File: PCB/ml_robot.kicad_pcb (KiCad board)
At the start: 2 copper layers, 85.4 x 100 mm, 17 parts, among them J1 lidar_conn, J2 Motor1, J3 Motor2, J4 jmp_alim, J5 ext_power, SW1 SW_Push, U1 ESP32-S3-DEVKITC-1-N8R2, U3 TB6612FNG

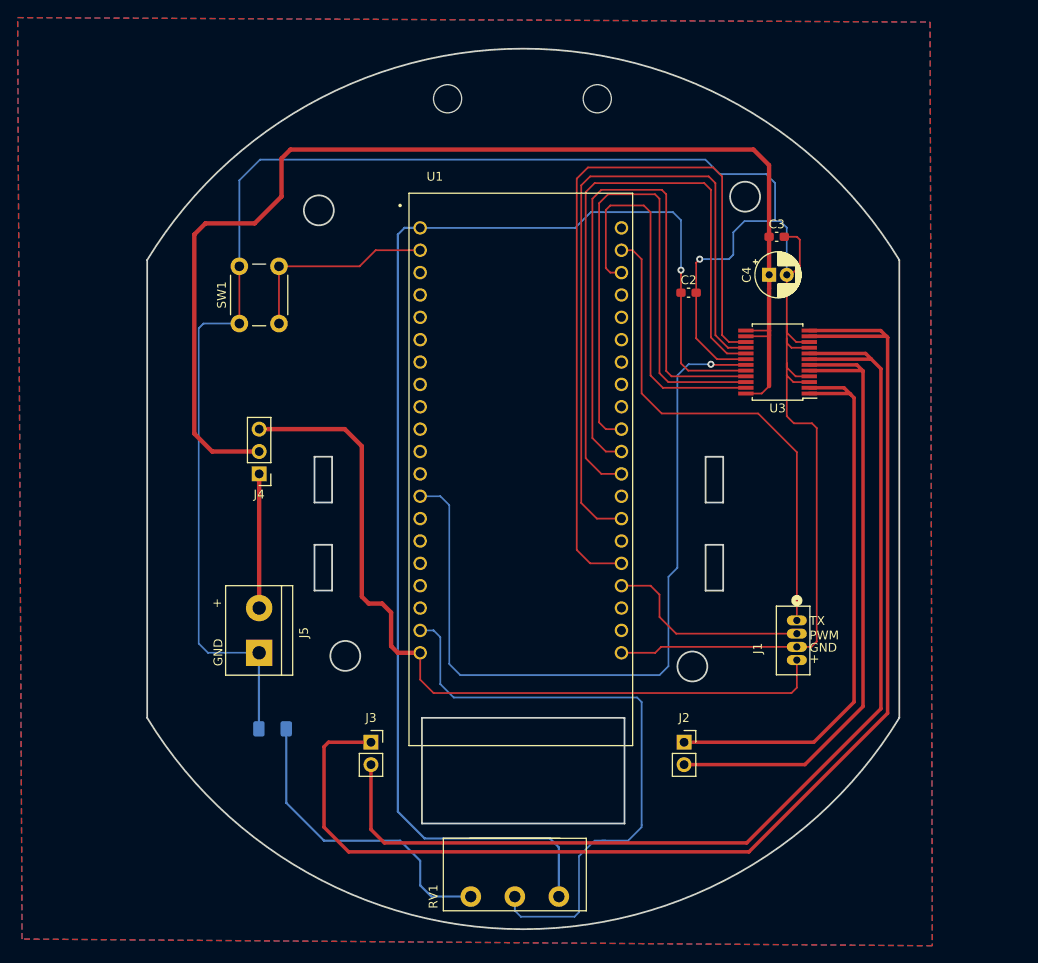
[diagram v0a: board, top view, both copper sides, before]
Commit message: Adding exclusion zones
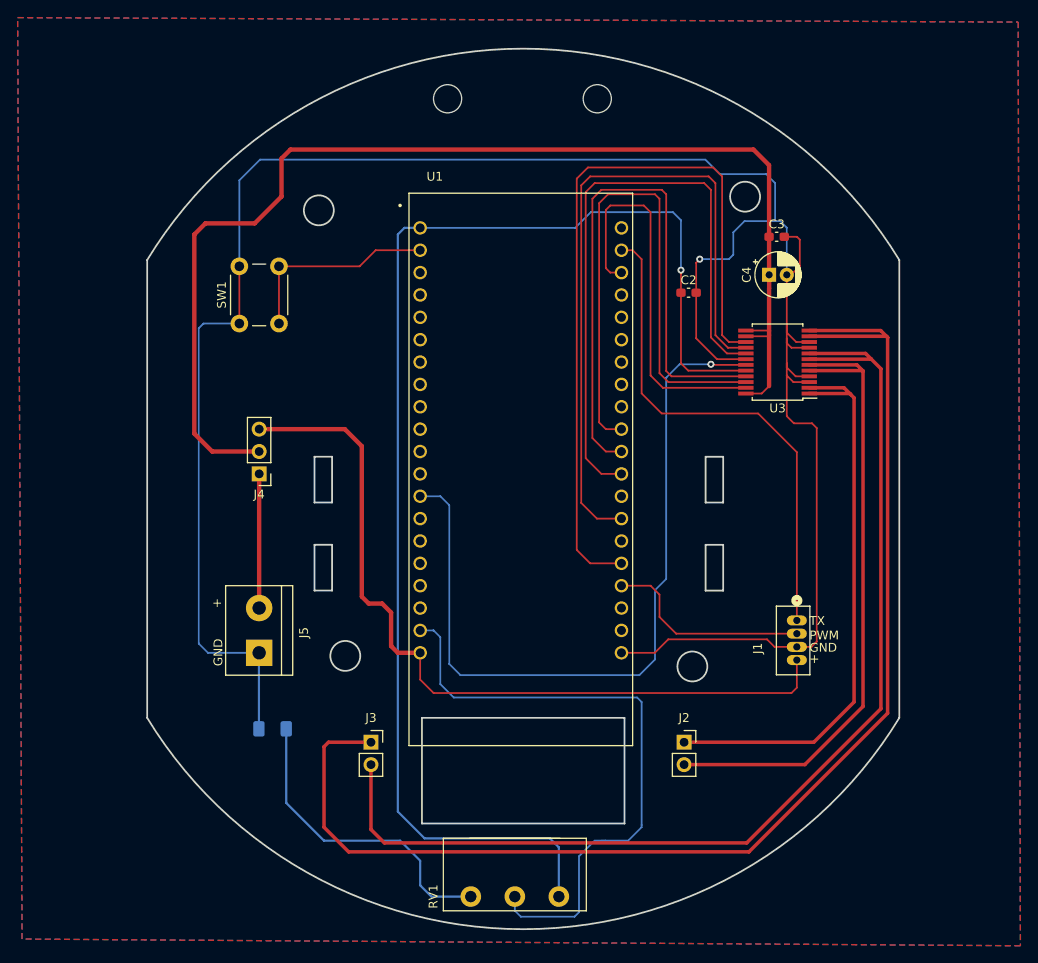
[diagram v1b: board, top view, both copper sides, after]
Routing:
- net /STBY_motor: track 89.4 -> 88.6 mm
- net GND: track 261.9 -> 262.7 mm
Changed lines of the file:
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@@
   )
   (paper "A4")
+  (title_block
+    (title "machine_learning_robot")
+    (date "2023-10-05")
+    (rev "A1")
+    (company "Institute for Future Technologies")
+    (comment 2 "Co-Author : Nicolas STAS")
+    (comment 3 "Author : Matthieu SEGUI")
+  )
   (layers
     (0 "F.Cu" signal)
@@
   (segment (start 139.2682 71.882) (end 148.59 71.882) (width 0.2) (layer "B.Cu") (net 1))
   (segment (start 162.534 90.525) (end 161.519888 89.510888) (width 0.2) (layer "F.Cu") (net 2))
+  (segment (start 142.748 121.922) (end 146.5306 121.922) (width 0.2) (layer "F.Cu") (net 2))
   (segment (start 164.3241 121.2481) (end 164.9222 120.65) (width 0.2) (layer "F.Cu") (net 2))
   (segment (start 161.519888 95.048088) (end 161.519888 90.425288) (width 0.2) (layer "F.Cu") (net 2))
   (segment (start 164.075 87.275) (end 162.0526 87.275) (width 0.2) (layer "F.Cu") (net 2))
+  (segment (start 159.2834 120.396) (end 160.1355 121.2481) (width 0.2) (layer "F.Cu") (net 2))
   (segment (start 151.2305 86.2065) (end 151.2305 81.026) (width 0.2) (layer "F.Cu") (net 2))
+  (segment (start 160.1355 121.2481) (end 162.6645 121.2481) (width 0.2) (layer "F.Cu") (net 2))
   (segment (start 164.3888 95.8596) (end 162.3314 95.8596) (width 0.2) (layer "F.Cu") (net 2))
   (segment (start 99.35 84.53) (end 99.35 78.03) (width 0.2) (layer "F.Cu") (net 2))
@@
   (segment (start 156.875 88.575) (end 153.599 88.575) (width 0.2) (layer "F.Cu") (net 2))
   (segment (start 162.5964 86.625) (end 161.519888 85.548488) (width 0.2) (layer "F.Cu") (net 2))
-  (segment (start 146.5814 121.922) (end 142.748 121.922) (width 0.2) (layer "F.Cu") (net 2))
+  (segment (start 146.5306 121.922) (end 148.0566 120.396) (width 0.2) (layer "F.Cu") (net 2))
   (segment (start 161.519888 90.425288) (end 161.519888 89.0524) (width 0.2) (layer "F.Cu") (net 2))
   (segment (start 162.6645 121.2481) (end 164.3241 121.2481) (width 0.2) (layer "F.Cu") (net 2))
+  (segment (start 162.6645 121.2481) (end 162.6626 121.25) (width 0.2) (layer "F.Cu") (net 2))
+  (segment (start 148.0566 120.396) (end 159.2834 120.396) (width 0.2) (layer "F.Cu") (net 2))
   (segment (start 161.519888 84.6836) (end 161.519888 78.994) (width 0.2) (layer "F.Cu") (net 2))
   (segment (start 151.2305 77.6235) (end 151.638 77.216) (width 0.2) (layer "F.Cu") (net 2))
@@
   (segment (start 161.237 74.676) (end 162.676 74.676) (width 0.2) (layer "F.Cu") (net 2))
   (segment (start 161.519888 86.742288) (end 161.519888 84.6836) (width 0.2) (layer "F.Cu") (net 2))
-  (segment (start 147.2553 121.2481) (end 146.5814 121.922) (width 0.2) (layer "F.Cu") (net 2))
   (segment (start 164.075 90.525) (end 162.534 90.525) (width 0.2) (layer "F.Cu") (net 2))
   (segment (start 164.075 86.625) (end 162.5964 86.625) (width 0.2) (layer "F.Cu") (net 2))
@@
   (segment (start 162.0526 87.275) (end 161.519888 86.742288) (width 0.2) (layer "F.Cu") (net 2))
   (segment (start 163 78) (end 162.006 78.994) (width 0.2) (layer "F.Cu") (net 2))
-  (segment (start 162.6645 121.2481) (end 147.2553 121.2481) (width 0.2) (layer "F.Cu") (net 2))
   (segment (start 161.519888 89.510888) (end 161.519888 89.0524) (width 0.2) (layer "F.Cu") (net 2))
   (segment (start 164.9222 96.393) (end 164.3888 95.8596) (width 0.2) (layer "F.Cu") (net 2))
@@
   (segment (start 152.979 89.225) (end 152.908 89.154) (width 0.2) (layer "F.Cu") (net 29))
   (via (at 152.908 89.154) (size 0.8) (drill 0.4) (layers "F.Cu" "B.Cu") (net 29))
+  (segment (start 152.908 89.154) (end 149.352 89.154) (width 0.2) (layer "B.Cu") (net 29))
+  (segment (start 123.19 105.156) (end 122.176 104.142) (width 0.2) (layer "B.Cu") (net 29))
+  (segment (start 147.828 90.678) (end 147.828 113.538) (width 0.2) (layer "B.Cu") (net 29))
+  (segment (start 146.558 122.682) (end 144.78 124.46) (width 0.2) (layer "B.Cu") (net 29))
+  (segment (start 147.828 113.538) (end 146.558 114.808) (width 0.2) (layer "B.Cu") (net 29))
+  (segment (start 123.19 123.19) (end 123.19 105.156) (width 0.2) (layer "B.Cu") (net 29))
   (segment (start 124.46 124.46) (end 123.19 123.19) (width 0.2) (layer "B.Cu") (net 29))
-  (segment (start 149.098 90.424) (end 149.098 112.268) (width 0.2) (layer "B.Cu") (net 29))
-  (segment (start 152.908 89.154) (end 150.368 89.154) (width 0.2) (layer "B.Cu") (net 29))
-  (segment (start 150.368 89.154) (end 149.098 90.424) (width 0.2) (layer "B.Cu") (net 29))
-  (segment (start 149.098 112.268) (end 148.082 113.284) (width 0.2) (layer "B.Cu") (net 29))
+  (segment (start 144.78 124.46) (end 124.46 124.46) (width 0.2) (layer "B.Cu") (net 29))
   (segment (start 122.176 104.142) (end 119.888 104.142) (width 0.2) (layer "B.Cu") (net 29))
-  (segment (start 123.19 123.19) (end 123.19 105.156) (width 0.2) (layer "B.Cu") (net 29))
-  (segment (start 148.082 113.284) (end 148.082 123.444) (width 0.2) (layer "B.Cu") (net 29))
-  (segment (start 147.066 124.46) (end 124.46 124.46) (width 0.2) (layer "B.Cu") (net 29))
-  (segment (start 123.19 105.156) (end 122.176 104.142) (width 0.2) (layer "B.Cu") (net 29))
-  (segment (start 148.082 123.444) (end 147.066 124.46) (width 0.2) (layer "B.Cu") (net 29))
+  (segment (start 146.558 114.808) (end 146.558 122.682) (width 0.2) (layer "B.Cu") (net 29))
+  (segment (start 149.352 89.154) (end 147.828 90.678) (width 0.2) (layer "B.Cu") (net 29))
   (segment (start 141.48 78.742) (end 140.97 78.232) (width 0.2) (layer "F.Cu") (net 37))
   (segment (start 146.05 71.882) (end 146.05 90.424) (width 0.2) (layer "F.Cu") (net 37))
@@
   (segment (start 117.602 143.256) (end 108.966 143.256) (width 0.25) (layer "B.Cu") (net 47))
   (segment (start 119.888 145.542) (end 117.602 143.256) (width 0.25) (layer "B.Cu") (net 47))
+  (zone (net 0) (net_name "") (layers "F&B.Cu") (hatch edge 0.5)
+    (connect_pads (clearance 0))
+    (min_thickness 0.25) (filled_areas_thickness no)
+    (keepout (tracks not_allowed) (vias not_allowed) (pads not_allowed) (copperpour not_allowed) (footprints allowed))
+    (fill (thermal_gap 0.5) (thermal_bridge_width 0.5))
+    (polygon
+      (pts
+        (xy 153.416 120.904)
+        (xy 153.416 125.984)
+        (xy 148.082 125.984)
+        (xy 148.082 120.904)
+      )
+    )
+  )
+  (zone (net 0) (net_name "") (layers "F&B.Cu") (hatch edge 0.5)
+    (connect_pads (clearance 0))
+    (min_thickness 0.25) (filled_areas_thickness no)
+    (keepout (tracks not_allowed) (vias not_allowed) (pads not_allowed) (copperpour not_allowed) (footprints allowed))
+    (fill (thermal_gap 0.5) (thermal_bridge_width 0.5))
+    (polygon
+      (pts
+        (xy 158.75 67.31)
+        (xy 158.75 72.644)
+        (xy 154.686 72.644)
+        (xy 154.686 67.31)
+      )
+    )
+  )
+  (zone (net 0) (net_name "") (layers "F&B.Cu") (hatch edge 0.5)
+    (connect_pads (clearance 0))
+    (min_thickness 0.25) (filled_areas_thickness no)
+    (keepout (tracks not_allowed) (vias not_allowed) (pads not_allowed) (copperpour not_allowed) (footprints allowed))
+    (fill (thermal_gap 0.5) (thermal_bridge_width 0.5))
+    (polygon
+      (pts
+        (xy 114.046 119.634)
+        (xy 114.046 124.714)
+        (xy 108.712 124.714)
+        (xy 108.712 119.634)
+      )
+    )
+  )
   (zone (net 2) (net_name "GND") (layers "F&B.Cu") (hatch edge 0.5)
     (connect_pads (clearance 0.508))
@@
       (pts
         (xy 74.168 49.784)
-        (xy 177.8 50.292)
-        (xy 178.054 155.194)
+        (xy 187.8 50.292)
+        (xy 188.054 155.194)
         (xy 74.676 154.432)
       )
     )
+  )
+  (zone (net 0) (net_name "") (layers "F&B.Cu") (hatch edge 0.5)
+    (connect_pads (clearance 0))
+    (min_thickness 0.25) (filled_areas_thickness no)
+    (keepout (tracks not_allowed) (vias not_allowed) (pads not_allowed) (copperpour not_allowed) (footprints allowed))
+    (fill (thermal_gap 0.5) (thermal_bridge_width 0.5))
+    (polygon
+      (pts
+        (xy 110.998 69.088)
+        (xy 110.998 74.168)
+        (xy 105.664 74.168)
+        (xy 105.664 69.088)
+      )
+    )

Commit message: PCB version to fab
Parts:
- removed C4: 10uF, Capacitor_THT:CP_Radial_D5.0mm_P2.00mm
- removed R1: 100kΩ, Resistor_SMD:R_1206_3216Metric_Pad1.30x1.75mm_HandSolder
- removed the REF** at (140.0, 59.0)
- removed the REF** at (123.0, 59.0)
- added C1: 10u, Capacitor_SMD:C_0805_2012Metric_Pad1.18x1.45mm_HandSolder, F.Cu at (160.3, 79.0)
- added REF**: MountingHole_3.2mm_M3, MountingHole:MountingHole_3.2mm_M3, F.Cu at (123.5, 59.4)
- added REF**: MountingHole_3.2mm_M3, MountingHole:MountingHole_3.2mm_M3, F.Cu at (140.5, 59.4)
- C2, C3: footprint Capacitor_SMD:C_0603_1608Metric_Pad1.08x0.95mm_HandSolder -> Capacitor_SMD:C_0805_2012Metric_Pad1.18x1.45mm_HandSolder
- U1: footprint ESP32-S3-DEVKITC-1-N8R2:XCVR_ESP32-S3-DEVKITC-1-N8R2 -> custom_esp32:XCVR_ESP32-S3-DEVKITC-1-N8R2
- moved J3 1.24 mm to (113.1, 132.1)
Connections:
- RV1 pad 3: Net-(R1-Pad1) -> GND
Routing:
- net /STBY_motor: track 88.6 -> 45.7 mm
- net Net-(R1-Pad1): track 35.4 -> 0.00 mm
- net GND: track 262.7 -> 282.5 mm
- net Net-(J3-Pin_1): track 147.2 -> 139.2 mm
- net /v_motor: track 136.7 -> 131.9 mm
- net +3V3: track 148.7 -> 144.1 mm
- net +5V: track 91.1 -> 86.9 mm
- net Net-(U1-GPIO14): track 70.6 -> 67.4 mm
- net Net-(U1-RST): track 23.3 -> 20.8 mm
- net Net-(J2-Pin_1): track 66.1 -> 63.7 mm
- net Net-(J2-Pin_2): track 73.7 -> 71.6 mm
- net Net-(J3-Pin_2): track 126.7 -> 125.2 mm
- net /lidar_pwm: track 23.7 -> 22.2 mm
- net /control_M1_B: track 65.3 -> 64.8 mm
